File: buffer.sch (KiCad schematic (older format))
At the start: 11 parts, among them U1 LFE5U-12F-8BG256C, U10 74LVC245, U11 74LVC245, U12 TXS0104E, U3 74LVC245, U4 74LVC245, U5 74LVC245, U6 74LVC245, U7 74LVC245, U8 74LVC245, U9 74LVC245

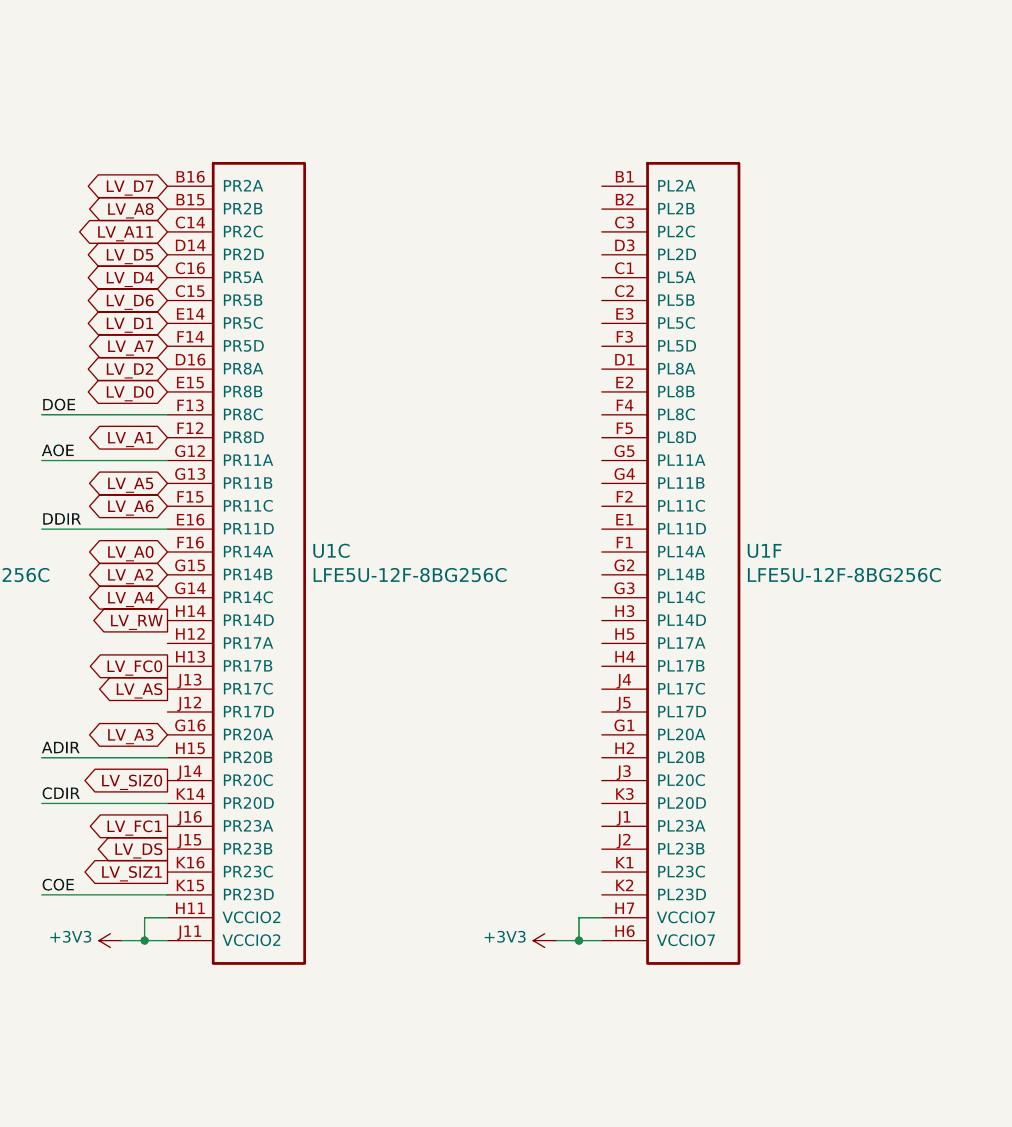
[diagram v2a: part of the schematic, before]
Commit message: add sdram connections
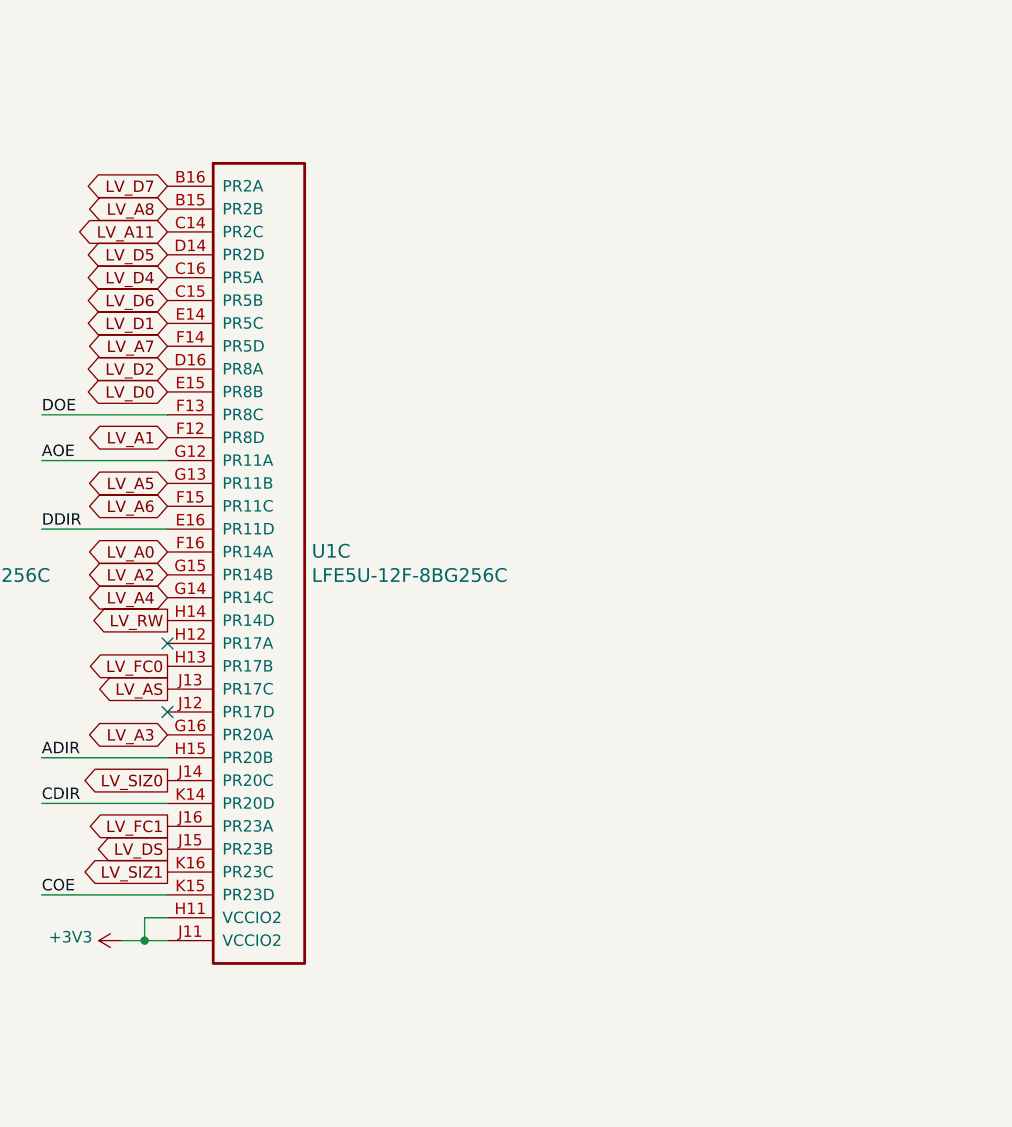
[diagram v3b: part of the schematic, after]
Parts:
- removed unit 6 of U1
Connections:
- no-connect marks 5 -> 7
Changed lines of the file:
@@
 Text Label 8950 4400 0    50   ~ 0
 DDIR
-Wire Wire Line
-	11400 6100 11300 6100
-Wire Wire Line
-	11300 6100 11300 6200
-Wire Wire Line
-	11400 6200 11300 6200
-$Comp
-L ecp5:LFE5U-12F-8BG256C U?
-U 6 1 5C32A4F9
-P 11400 2900
-AR Path="/5C254FCC/5C32A4F9" Ref="U?"  Part="6"
-AR Path="/5C35F270/5C32A4F9" Ref="U?"  Part="6"
-AR Path="/5C32A4F9" Ref="U?"  Part="6"
-AR Path="/5C2FB052/5C32A4F9" Ref="U?"  Part="6"
-AR Path="/5C254FC9/5C32A4F9" Ref="U1"  Part="6"
-F 0 "U1" H 12031 1303 60  0000 L CNN
-F 1 "LFE5U-12F-8BG256C" H 12031 1197 60  0000 L CNN
-F 2 "Package_BGA:BGA-256_14.0x14.0mm_Layout16x16_P0.8mm_Ball0.45mm_Pad0.32mm_NSMD" H 11600 2950 60  0001 L CNN
-F 3 "" H 11400 2900 50  0001 C CNN
-	6    11400 2900
-	1    0    0    -1
-$EndComp
-Wire Wire Line
-	11200 6200 11300 6200
-Connection ~ 11300 6200
-$Comp
-L power:+3V3 #PWR?
-U 1 1 5C32A502
-P 11200 6200
-AR Path="/5C35F270/5C32A502" Ref="#PWR?"  Part="1"
-AR Path="/5C32A502" Ref="#PWR?"  Part="1"
-AR Path="/5C2FB052/5C32A502" Ref="#PWR?"  Part="1"
-AR Path="/5C254FC9/5C32A502" Ref="#PWR0166"  Part="1"
-F 0 "#PWR0166" H 11200 6050 50  0001 C CNN
-F 1 "+3V3" V 11215 6328 50  0000 L CNN
-F 2 "" H 11200 6200 50  0001 C CNN
-F 3 "" H 11200 6200 50  0001 C CNN
-	1    11200 6200
-	0    -1   -1   0
-$EndComp
 Text GLabel 4700 1600 0    50   Output ~ 0
 LV_DSACK1
@@
 NoConn ~ 7500 4200
 NoConn ~ 7500 3600
+NoConn ~ 9500 4900
+NoConn ~ 9500 5200
 $EndSCHEMATC
